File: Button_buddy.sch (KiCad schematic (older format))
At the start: 8 parts

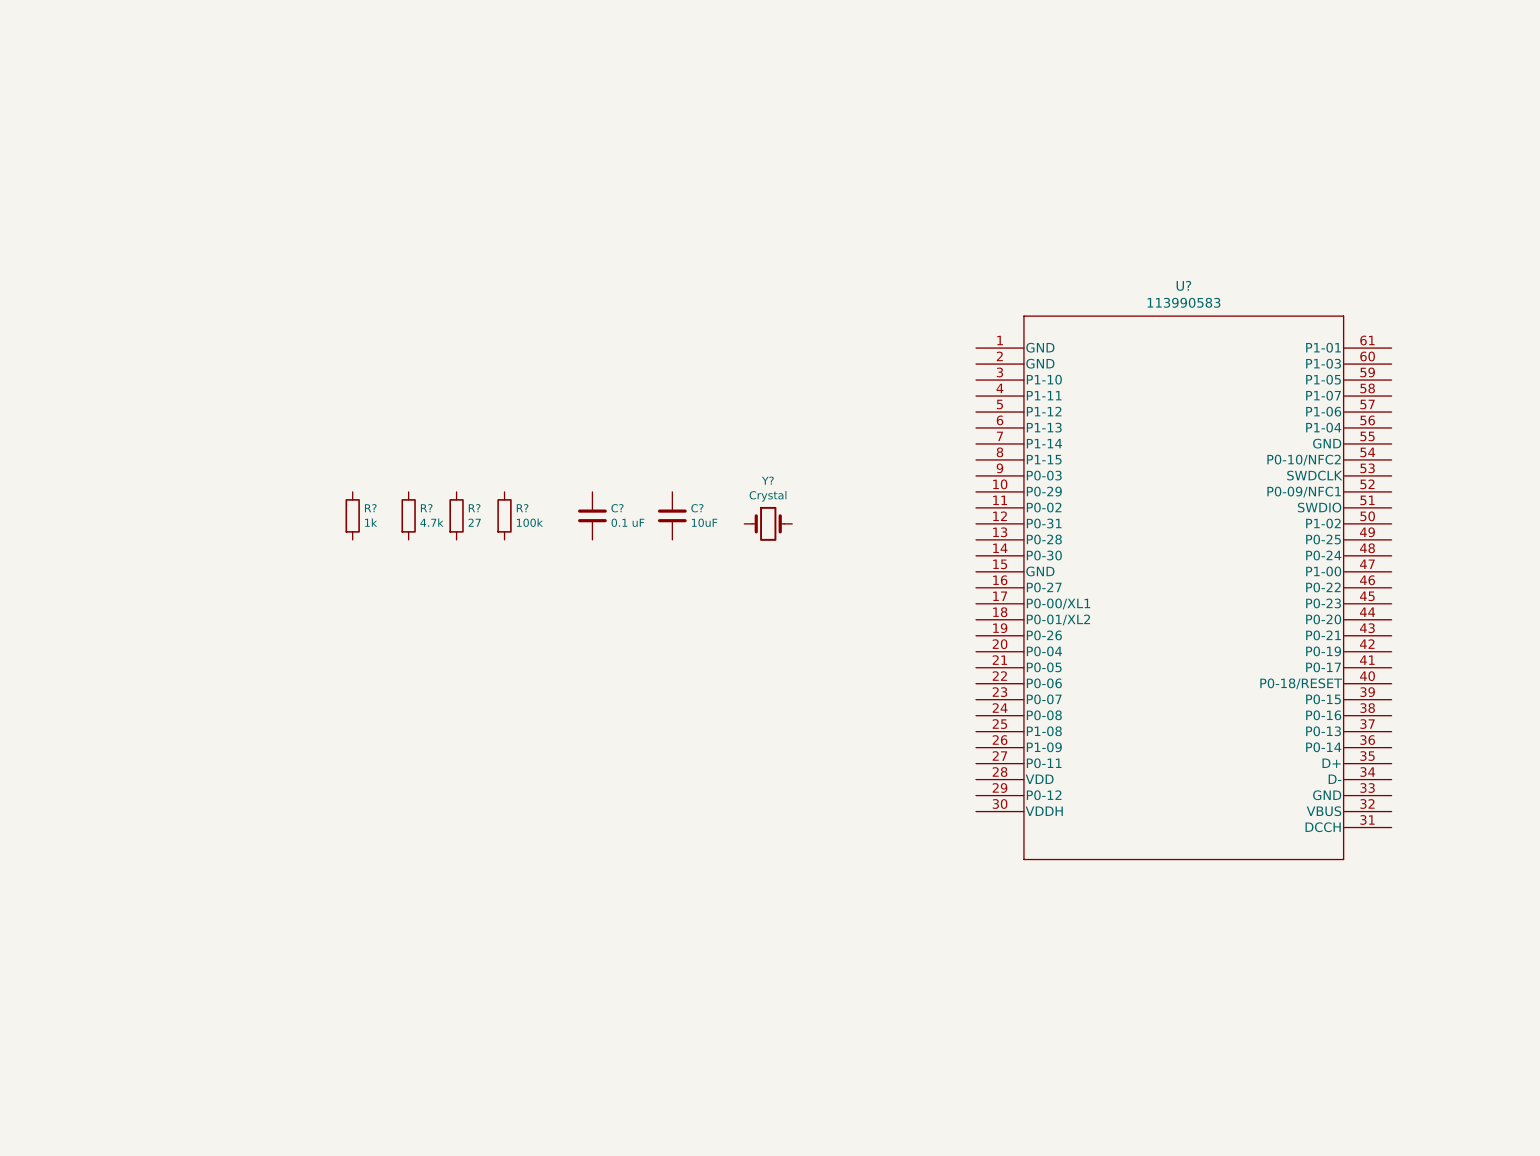
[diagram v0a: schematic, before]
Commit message: Added new symbols and footprints for electrical components
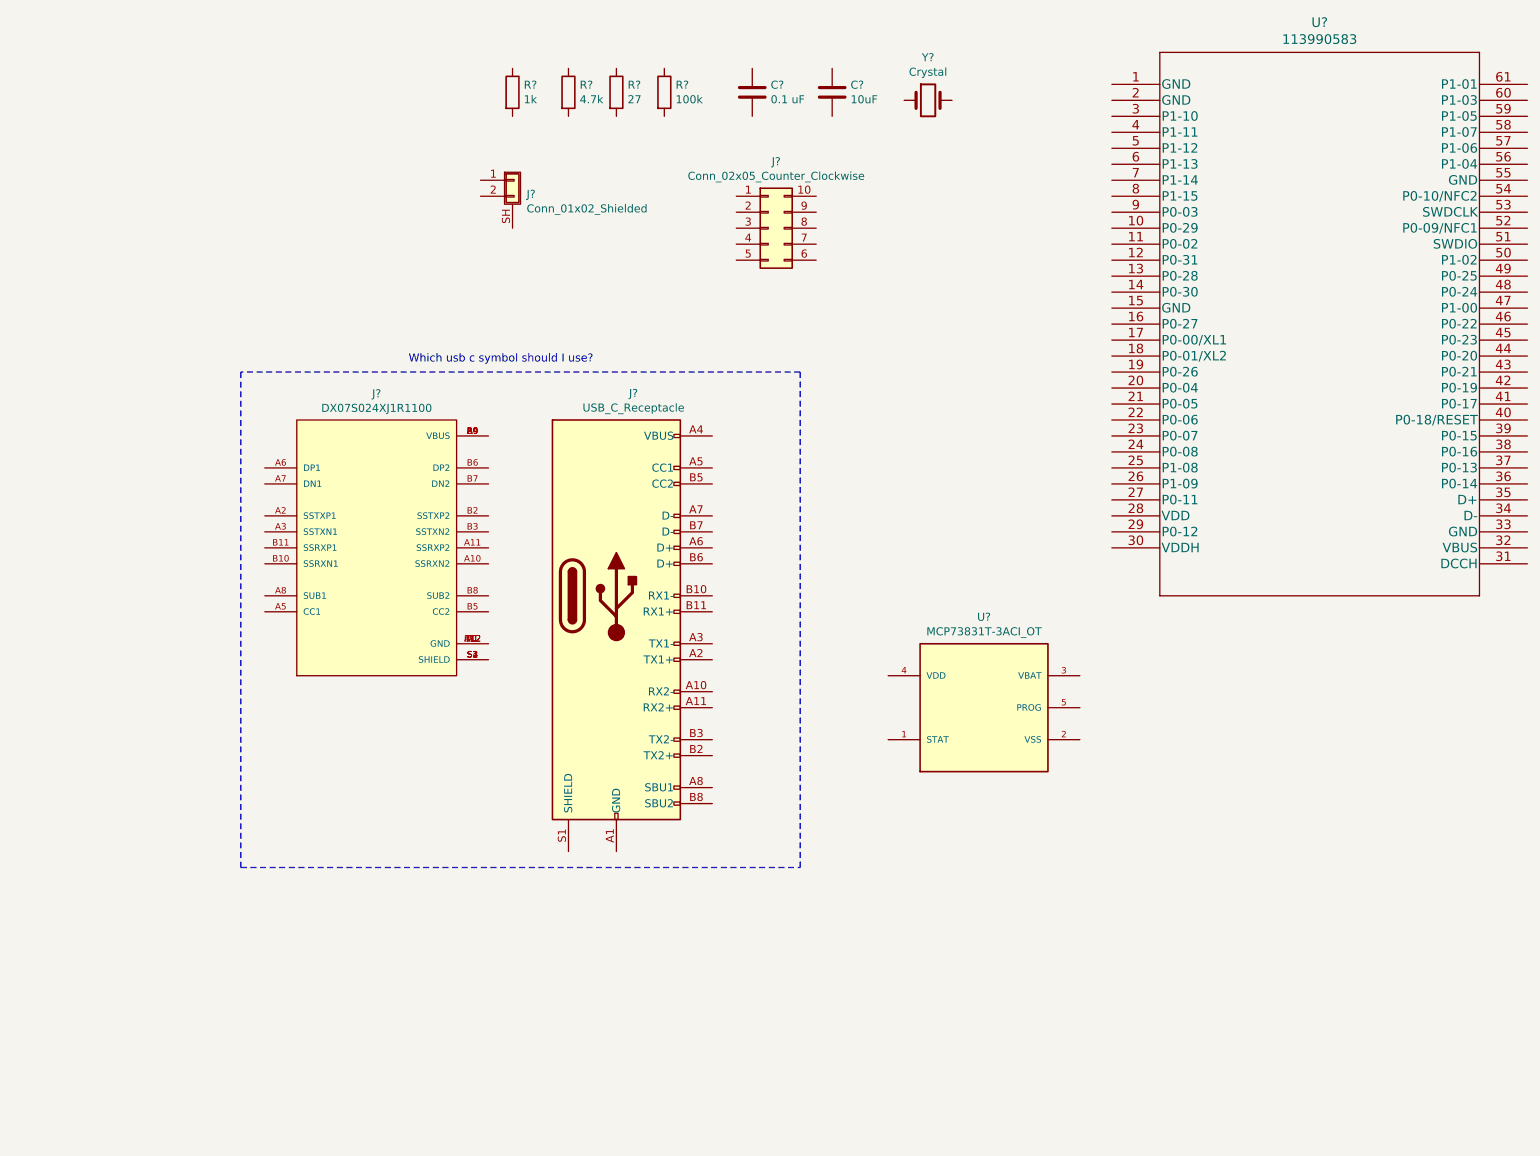
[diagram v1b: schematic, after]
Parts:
- added J?: Conn_01x02_Shielded, symbol Connector_Generic_Shielded:Conn_01x02_Shielded
- added J?: Conn_02x05_Counter_Clockwise, symbol Connector_Generic:Conn_02x05_Counter_Clockwise
- added J?: DX07S024XJ1R1100, JAE_DX07S024XJ1R1100, symbol USB_C_REC_CONN_24_TH:DX07S024XJ1R1100
- added J?: USB_C_Receptacle, symbol Connector:USB_C_Receptacle
- added U?: MCP73831T-3ACI_OT, SOT23-5, symbol MCP73831T-3ACI_OT:MCP73831T-3ACI_OT
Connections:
- new net: J?.A1 (GND), J?.A12 (GND), J?.B1 (GND), J?.B12 (GND) (x2)
- new net: J?.A4 (VBUS), J?.A9 (VBUS), J?.B4 (VBUS), J?.B9 (VBUS) (x2)
- new net: J?.S1 (SHIELD), J?.S2 (SHIELD), J?.S3 (SHIELD), J?.S4 (SHIELD)
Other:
- note added: "Which usb c symbol should I use?"
- moved on the sheet: C?, R?, U?, Y?
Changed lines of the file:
@@
 L Device:R R?
 U 1 1 60391BC0
-P 2850 3650
-F 0 "R?" H 2920 3696 50  0000 L CNN
-F 1 "1k" H 2920 3605 50  0000 L CNN
-F 2 "" V 2780 3650 50  0001 C CNN
-F 3 "~" H 2850 3650 50  0001 C CNN
-	1    2850 3650
+P 3850 1000
+F 0 "R?" H 3920 1046 50  0000 L CNN
+F 1 "1k" H 3920 955 50  0000 L CNN
+F 2 "" V 3780 1000 50  0001 C CNN
+F 3 "~" H 3850 1000 50  0001 C CNN
+	1    3850 1000
 	1    0    0    -1
 $EndComp
@@
 L Device:R R?
 U 1 1 60391E85
-P 3200 3650
-F 0 "R?" H 3270 3696 50  0000 L CNN
-F 1 "4.7k" H 3270 3605 50  0000 L CNN
-F 2 "" V 3130 3650 50  0001 C CNN
-F 3 "~" H 3200 3650 50  0001 C CNN
-	1    3200 3650
+P 4200 1000
+F 0 "R?" H 4270 1046 50  0000 L CNN
+F 1 "4.7k" H 4270 955 50  0000 L CNN
+F 2 "" V 4130 1000 50  0001 C CNN
+F 3 "~" H 4200 1000 50  0001 C CNN
+	1    4200 1000
 	1    0    0    -1
 $EndComp
@@
 L Device:R R?
 U 1 1 60392519
-P 3500 3650
-F 0 "R?" H 3570 3696 50  0000 L CNN
-F 1 "27" H 3570 3605 50  0000 L CNN
-F 2 "" V 3430 3650 50  0001 C CNN
-F 3 "~" H 3500 3650 50  0001 C CNN
-	1    3500 3650
+P 4500 1000
+F 0 "R?" H 4570 1046 50  0000 L CNN
+F 1 "27" H 4570 955 50  0000 L CNN
+F 2 "" V 4430 1000 50  0001 C CNN
+F 3 "~" H 4500 1000 50  0001 C CNN
+	1    4500 1000
 	1    0    0    -1
 $EndComp
@@
 L Device:R R?
 U 1 1 603926C1
-P 3800 3650
-F 0 "R?" H 3870 3696 50  0000 L CNN
-F 1 "100k" H 3870 3605 50  0000 L CNN
-F 2 "" V 3730 3650 50  0001 C CNN
-F 3 "~" H 3800 3650 50  0001 C CNN
-	1    3800 3650
+P 4800 1000
+F 0 "R?" H 4870 1046 50  0000 L CNN
+F 1 "100k" H 4870 955 50  0000 L CNN
+F 2 "" V 4730 1000 50  0001 C CNN
+F 3 "~" H 4800 1000 50  0001 C CNN
+	1    4800 1000
 	1    0    0    -1
 $EndComp
@@
 L Device:C C?
 U 1 1 603A75AC
-P 4350 3650
-F 0 "C?" H 4465 3696 50  0000 L CNN
-F 1 "0.1 uF" H 4465 3605 50  0000 L CNN
-F 2 "" H 4388 3500 50  0001 C CNN
-F 3 "~" H 4350 3650 50  0001 C CNN
-	1    4350 3650
+P 5350 1000
+F 0 "C?" H 5465 1046 50  0000 L CNN
+F 1 "0.1 uF" H 5465 955 50  0000 L CNN
+F 2 "" H 5388 850 50  0001 C CNN
+F 3 "~" H 5350 1000 50  0001 C CNN
+	1    5350 1000
 	1    0    0    -1
 $EndComp
@@
 L Device:C C?
 U 1 1 603A8122
-P 4850 3650
-F 0 "C?" H 4965 3696 50  0000 L CNN
-F 1 "10uF" H 4965 3605 50  0000 L CNN
-F 2 "" H 4888 3500 50  0001 C CNN
-F 3 "~" H 4850 3650 50  0001 C CNN
-	1    4850 3650
+P 5850 1000
+F 0 "C?" H 5965 1046 50  0000 L CNN
+F 1 "10uF" H 5965 955 50  0000 L CNN
+F 2 "" H 5888 850 50  0001 C CNN
+F 3 "~" H 5850 1000 50  0001 C CNN
+	1    5850 1000
 	1    0    0    -1
 $EndComp
@@
 L Device:Crystal Y?
 U 1 1 603A7C4C
-P 5450 3700
-F 0 "Y?" H 5450 3968 50  0000 C CNN
-F 1 "Crystal" H 5450 3877 50  0000 C CNN
-F 2 "" H 5450 3700 50  0001 C CNN
-F 3 "~" H 5450 3700 50  0001 C CNN
-	1    5450 3700
+P 6450 1050
+F 0 "Y?" H 6450 1318 50  0000 C CNN
+F 1 "Crystal" H 6450 1227 50  0000 C CNN
+F 2 "" H 6450 1050 50  0001 C CNN
+F 3 "~" H 6450 1050 50  0001 C CNN
+	1    6450 1050
 	1    0    0    -1
 $EndComp
@@
 L Nordic_MDBT50Q:113990583 U?
 U 1 1 603B9C59
-P 6750 2600
-F 0 "U?" H 8050 2987 60  0000 C CNN
-F 1 "113990583" H 8050 2881 60  0000 C CNN
-F 2 "113990583_SEE" H 8050 2840 60  0001 C CNN
-F 3 "" H 6750 2600 60  0000 C CNN
-	1    6750 2600
+P 7600 950
+F 0 "U?" H 8900 1337 60  0000 C CNN
+F 1 "113990583" H 8900 1231 60  0000 C CNN
+F 2 "113990583_SEE" H 8900 1190 60  0001 C CNN
+F 3 "" H 7600 950 60  0000 C CNN
+	1    7600 950
 	1    0    0    -1
 $EndComp
+$Comp
+L Connector_Generic_Shielded:Conn_01x02_Shielded J?
+U 1 1 603FDDF4
+P 3850 1550
+F 0 "J?" H 3938 1463 50  0000 L CNN
+F 1 "Conn_01x02_Shielded" H 3938 1372 50  0000 L CNN
+F 2 "" H 3850 1550 50  0001 C CNN
+F 3 "~" H 3850 1550 50  0001 C CNN
+	1    3850 1550
+	1    0    0    -1
+$EndComp
+$Comp
+L Connector_Generic:Conn_02x05_Counter_Clockwise J?
+U 1 1 60400D0D
+P 5450 1850
+F 0 "J?" H 5500 2267 50  0000 C CNN
+F 1 "Conn_02x05_Counter_Clockwise" H 5500 2176 50  0000 C CNN
+F 2 "" H 5450 1850 50  0001 C CNN
+F 3 "~" H 5450 1850 50  0001 C CNN
+	1    5450 1850
+	1    0    0    -1
+$EndComp
+$Comp
+L USB_C_REC_CONN_24_TH:DX07S024XJ1R1100 J?
+U 1 1 6040B8A2
+P 3000 3850
+F 0 "J?" H 3000 4815 50  0000 C CNN
+F 1 "DX07S024XJ1R1100" H 3000 4724 50  0000 C CNN
+F 2 "JAE_DX07S024XJ1R1100" H 3000 3850 50  0001 L BNN
+F 3 "" H 3000 3850 50  0001 L BNN
+F 4 "1" H 3000 3850 50  0001 L BNN "PARTREV"
+F 5 "JAE" H 3000 3850 50  0001 L BNN "MANUFACTURER"
+F 6 "Manufacturer recommendations" H 3000 3850 50  0001 L BNN "STANDARD"
+F 7 "3.34mm" H 3000 3850 50  0001 L BNN "MAXIMUM_PACKAGE_HEIGHT"
+	1    3000 3850
+	1    0    0    -1
+$EndComp
+$Comp
+L Connector:USB_C_Receptacle J?
+U 1 1 6040DD58
+P 4500 4150
+F 0 "J?" H 4607 5417 50  0000 C CNN
+F 1 "USB_C_Receptacle" H 4607 5326 50  0000 C CNN
+F 2 "" H 4650 4150 50  0001 C CNN
+F 3 "https://www.usb.org/sites/default/files/documents/usb_type-c.zip" H 4650 4150 50  0001 C CNN
+	1    4500 4150
+	1    0    0    -1
+$EndComp
+Text Notes 3200 2700 0    50   ~ 0
+Which usb c symbol should I use?
+Wire Notes Line
+	2150 2750 2150 5850
+Wire Notes Line
+	2150 5850 5650 5850
+Wire Notes Line
+	5650 5850 5650 2750
+Wire Notes Line
+	5650 2750 2150 2750
+$Comp
+L MCP73831T-3ACI_OT:MCP73831T-3ACI_OT U?
+U 1 1 6041B049
+P 6800 4850
+F 0 "U?" H 6800 5417 50  0000 C CNN
+F 1 "MCP73831T-3ACI_OT" H 6800 5326 50  0000 C CNN
+F 2 "SOT23-5" H 6800 4850 50  0001 L BNN
+F 3 "" H 6800 4850 50  0001 L BNN
+	1    6800 4850
+	1    0    0    -1
+$EndComp

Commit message: Added some wiring for the lipo charging and jst ph lipo input and changed mcp73831T symbol
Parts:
- removed J?: DX07S024XJ1R1100, JAE_DX07S024XJ1R1100, symbol USB_C_REC_CONN_24_TH:DX07S024XJ1R1100
- added C?: 10uF, symbol Device:C
- added D?: LED, symbol Device:LED
- added R?: 1k, symbol Device:R
- added R?: 4.7k, symbol Device:R
- added R? (x2): 100k, symbol Device:R
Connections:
- net GND: now reaches J?.1 (Pin_1)
- net GND: now also U?.2 (VSS), C?.2, R?.1, R?.2
- net VBAT: now reaches J?.2 (Pin_2)
- net VBAT: now also U?.3 (VBAT), C?.1, R?.1
- net at U?.1 (STAT): now also R?.2
- net VBUS: now reaches U?.4 (VDD)
- net VBUS: now also D?.2 (A)
- net at U?.5 (PROG): now also R?.2
- new net: D?.1 (K), R?.1
- new net VDIV: R?.1, R?.2
- no-connect marks 0 -> 1
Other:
- note added: "JST PH LIPO INPUT"
- note added: "LIPO CHARGING"
- note removed: "Which usb c symbol should I use?"
- moved on the sheet: J?, U?
